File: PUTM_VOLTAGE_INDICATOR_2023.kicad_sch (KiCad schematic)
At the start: 29 parts

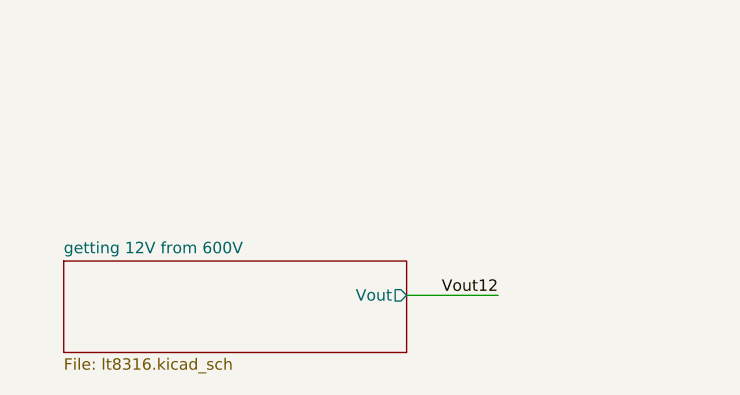
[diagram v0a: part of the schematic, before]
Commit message: change scheme of LT8316EFE and change mosfet symbol
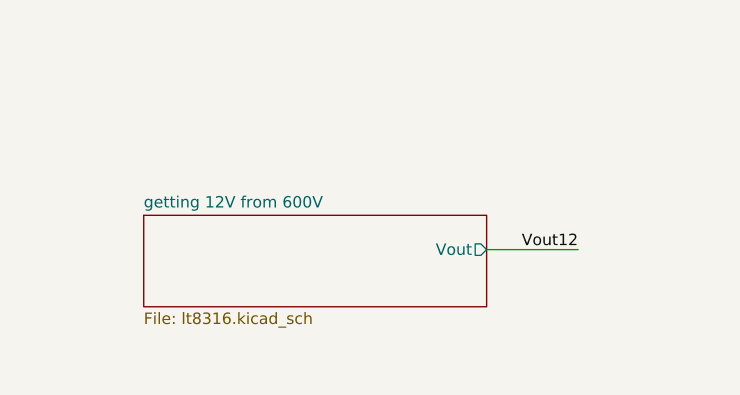
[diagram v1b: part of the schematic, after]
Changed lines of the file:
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@@
     (stroke (width 0) (type default) (color 0 0 0 0))
   )
-  (wire (pts (xy 57.15 175.26) (xy 67.31 175.26))
+  (wire (pts (xy 66.04 170.18) (xy 76.2 170.18))
     (stroke (width 0) (type default) (color 0 0 0 0))
   )
@@
     (effects (font (size 1.27 1.27)) (justify left bottom))
   )
-  (label "Vout12" (at 67.31 175.26 180)
+  (label "Vout12" (at 76.2 170.18 180)
     (effects (font (size 1.27 1.27)) (justify right bottom))
   )
@@
     (pin "1")
   )
-  (sheet (at 19.05 171.45) (size 38.1 10.16) (fields_autoplaced)
+  (sheet (at 27.94 166.37) (size 38.1 10.16) (fields_autoplaced)
     (stroke (width 0.1524) (type solid) (color 0 0 0 0))
     (fill (color 0 0 0 0.0000))
-    (property "Sheet name" "getting 12V from 600V" (id 0) (at 19.05 170.7384 0)
+    (property "Sheet name" "getting 12V from 600V" (id 0) (at 27.94 165.6584 0)
       (effects (font (size 1.27 1.27)) (justify left bottom))
     )
-    (property "Sheet file" "lt8316.kicad_sch" (id 1) (at 19.05 182.1946 0)
+    (property "Sheet file" "lt8316.kicad_sch" (id 1) (at 27.94 177.1146 0)
       (effects (font (size 1.27 1.27)) (justify left top))
     )
-    (pin "Vout" output (at 57.15 175.26 0)
+    (pin "Vout" output (at 66.04 170.18 0)
       (effects (font (size 1.27 1.27)) (justify right))
     )
@@
       (reference "#PWR?") (unit 1) (value "GND") (footprint "")
     )
+    (path "/cf374e18-b903-43ca-958b-fca5770ec61b/32e7c143-cc70-4ac4-97f7-77453f5f7f07"
+      (reference "#PWR?") (unit 1) (value "+VDC") (footprint "")
+    )
     (path "/4223f3f4-088d-4b9a-b16e-54b98ff9a1d3"
       (reference "#PWR?") (unit 1) (value "GND") (footprint "")
@@
       (reference "#PWR?") (unit 1) (value "+VDC") (footprint "")
     )
+    (path "/cf374e18-b903-43ca-958b-fca5770ec61b/558f1925-db51-40a5-9371-69be9ca78e10"
+      (reference "#PWR?") (unit 1) (value "GND") (footprint "")
+    )
     (path "/5b7feee9-3e0b-4567-88f5-c7d252aaf5c0"
       (reference "#PWR?") (unit 1) (value "+12V") (footprint "")
@@
       (reference "#PWR?") (unit 1) (value "+VDC") (footprint "")
     )
+    (path "/cf374e18-b903-43ca-958b-fca5770ec61b/c72ad2c8-75bd-4a1b-9496-8153431a76dd"
+      (reference "#PWR?") (unit 1) (value "GND") (footprint "")
+    )
     (path "/c838fd6c-06c5-492d-89ac-1fd1fa3897d4"
       (reference "#PWR?") (unit 1) (value "VCC") (footprint "")
@@
       (reference "#PWR?") (unit 1) (value "+12V") (footprint "")
     )
+    (path "/cf374e18-b903-43ca-958b-fca5770ec61b/e4996a15-9c7b-44e3-b2f2-01f8284846b2"
+      (reference "#PWR?") (unit 1) (value "GND") (footprint "")
+    )
     (path "/ec6155d8-6db3-4a50-a687-efa4cf3fb9c6"
       (reference "#PWR?") (unit 1) (value "GND") (footprint "")
@@
       (reference "0.1uF") (unit 1) (value "C") (footprint "")
     )
+    (path "/cf374e18-b903-43ca-958b-fca5770ec61b/6512fcfd-0e88-4a57-9170-2b4d1e9e185a"
+      (reference "0.1uF?") (unit 1) (value "C") (footprint "")
+    )
     (path "/2274b550-aef8-4476-a118-58107d10741d"
       (reference "C?") (unit 1) (value "2.2uF") (footprint "")
@@
       (reference "C?") (unit 1) (value "47uF") (footprint "")
     )
+    (path "/cf374e18-b903-43ca-958b-fca5770ec61b/3f6bfd71-6bce-4c99-bd68-922bfb83a1da"
+      (reference "C?") (unit 1) (value "10pF") (footprint "")
+    )
     (path "/cf374e18-b903-43ca-958b-fca5770ec61b/5056d3f2-c6d3-443f-aecd-c9ebfef5539c"
       (reference "C?") (unit 1) (value "100nF") (footprint "")
     )
+    (path "/cf374e18-b903-43ca-958b-fca5770ec61b/5b976bcd-7fe6-40cf-8a91-d330470a592a"
+      (reference "C?") (unit 1) (value "10uF") (footprint "")
+    )
     (path "/cf374e18-b903-43ca-958b-fca5770ec61b/5efacf5a-b103-469c-a71d-d6ed6b95c45d"
       (reference "C?") (unit 1) (value "100nF") (footprint "")
     )
+    (path "/cf374e18-b903-43ca-958b-fca5770ec61b/684025e0-d0bc-41d1-a713-7deaab9e1633"
+      (reference "C?") (unit 1) (value "47uF") (footprint "")
+    )
+    (path "/cf374e18-b903-43ca-958b-fca5770ec61b/cf62173b-3dc5-412e-a328-851c9eba7807"
+      (reference "C?") (unit 1) (value "100nF") (footprint "")
+    )
     (path "/cf374e18-b903-43ca-958b-fca5770ec61b/e533f7c5-34c4-4513-9f24-ddd1ccb1d81b"
       (reference "C?") (unit 1) (value "10pF") (footprint "")
@@
       (reference "C?") (unit 1) (value "2.2uF") (footprint "")
     )
+    (path "/cf374e18-b903-43ca-958b-fca5770ec61b/f3af4538-1c61-4dec-818c-ecf361cf4188"
+      (reference "C?") (unit 1) (value "100nF") (footprint "")
+    )
     (path "/cf374e18-b903-43ca-958b-fca5770ec61b/fd856d70-a228-45b6-bafe-4244511b43da"
       (reference "C?") (unit 1) (value "10uF") (footprint "")
@@
       (reference "D?") (unit 1) (value "DIODE") (footprint "")
     )
+    (path "/cf374e18-b903-43ca-958b-fca5770ec61b/8e24397d-5de2-4ffb-a482-80bf7b206b39"
+      (reference "D?") (unit 1) (value "US1K") (footprint "Diode_SMD:D_SMA")
+    )
     (path "/91897ede-6f44-4f3e-aa25-9e44a9bcbc0d"
       (reference "D?") (unit 1) (value "LED") (footprint "")
     )
+    (path "/cf374e18-b903-43ca-958b-fca5770ec61b/92a4bb15-3c41-4d86-8b01-0ce002af70c1"
+      (reference "D?") (unit 1) (value "US1K") (footprint "Diode_SMD:D_SMA")
+    )
     (path "/ad476781-3f83-4b0d-82bb-63d05393dcea"
       (reference "D?") (unit 1) (value "D_Zener") (footprint "")
@@
       (reference "D?") (unit 1) (value "LED") (footprint "")
     )
+    (path "/cf374e18-b903-43ca-958b-fca5770ec61b/e2426266-66c6-45c2-82b1-8cb37a277731"
+      (reference "D?") (unit 1) (value "DIODE") (footprint "")
+    )
     (path "/efffbf78-2a23-4c71-89c2-7b09495fb248"
       (reference "D?") (unit 1) (value "D_Zener") (footprint "")
@@
       (reference "D?") (unit 1) (value "US1K") (footprint "Diode_SMD:D_SMA")
     )
+    (path "/cf374e18-b903-43ca-958b-fca5770ec61b/dad6d136-bd1e-4494-a1d6-f69b7f63bdfa"
+      (reference "L?") (unit 1) (value "1mH") (footprint "")
+    )
     (path "/cf374e18-b903-43ca-958b-fca5770ec61b/facf2856-bf45-43c5-94eb-6ba4df7ce070"
       (reference "L?") (unit 1) (value "1mH") (footprint "")
@@
       (reference "M?") (unit 1) (value "MNMOS") (footprint "")
     )
+    (path "/cf374e18-b903-43ca-958b-fca5770ec61b/b886016f-513c-4ed6-805b-d3c85529adcb"
+      (reference "Q?") (unit 1) (value "Q_NMOS_GDS") (footprint "")
+    )
+    (path "/cf374e18-b903-43ca-958b-fca5770ec61b/0bf5e8c6-420a-4108-b6af-a1516a599ae1"
+      (reference "R?") (unit 1) (value "21.5k") (footprint "")
+    )
     (path "/0d6327f9-c706-469d-93b9-6ed83cf7370d"
       (reference "R?") (unit 1) (value "R4=300k") (footprint "")
@@
       (reference "R?") (unit 1) (value "22.1k") (footprint "")
     )
+    (path "/cf374e18-b903-43ca-958b-fca5770ec61b/3998addc-a70c-46f9-a60b-b4a696d22e54"
+      (reference "R?") (unit 1) (value "220mR") (footprint "")
+    )
+    (path "/cf374e18-b903-43ca-958b-fca5770ec61b/4cd7afc4-aeab-4fee-84c8-105654ee0db5"
+      (reference "R?") (unit 1) (value "2.49kR") (footprint "")
+    )
     (path "/cf374e18-b903-43ca-958b-fca5770ec61b/6215538f-5043-4302-9cc2-a18e15893de7"
       (reference "R?") (unit 1) (value "10kR") (footprint "")
@@
       (reference "R?") (unit 1) (value "R2=300k") (footprint "")
     )
+    (path "/cf374e18-b903-43ca-958b-fca5770ec61b/9e265a50-cd33-44ce-b896-405684d13d0c"
+      (reference "R?") (unit 1) (value "10kR") (footprint "")
+    )
     (path "/cf374e18-b903-43ca-958b-fca5770ec61b/9f4fddab-3d79-4c7c-97ad-d1227094eaff"
       (reference "R?") (unit 1) (value "220mR") (footprint "")
@@
       (reference "R?") (unit 1) (value "R3=100k") (footprint "")
     )
+    (path "/cf374e18-b903-43ca-958b-fca5770ec61b/a7accbdf-0597-40b2-9a61-7b33f248f0ff"
+      (reference "R?") (unit 1) (value "22.1k") (footprint "")
+    )
     (path "/ade8ddfd-444b-447a-8c15-b4c75b49afa4"
       (reference "R?") (unit 1) (value "10kR") (footprint "")
@@
       (reference "U?") (unit 1) (value "OPAMP") (footprint "")
     )
+    (path "/cf374e18-b903-43ca-958b-fca5770ec61b/5a37aa80-6a33-41f2-8f70-b377198a3006"
+      (reference "U?") (unit 1) (value "LT8316EFE") (footprint "TSSOP20_FE_BB_16_")
+    )
     (path "/6f6314b0-2ff3-49a8-aa6a-e4a7bd5d24fe"

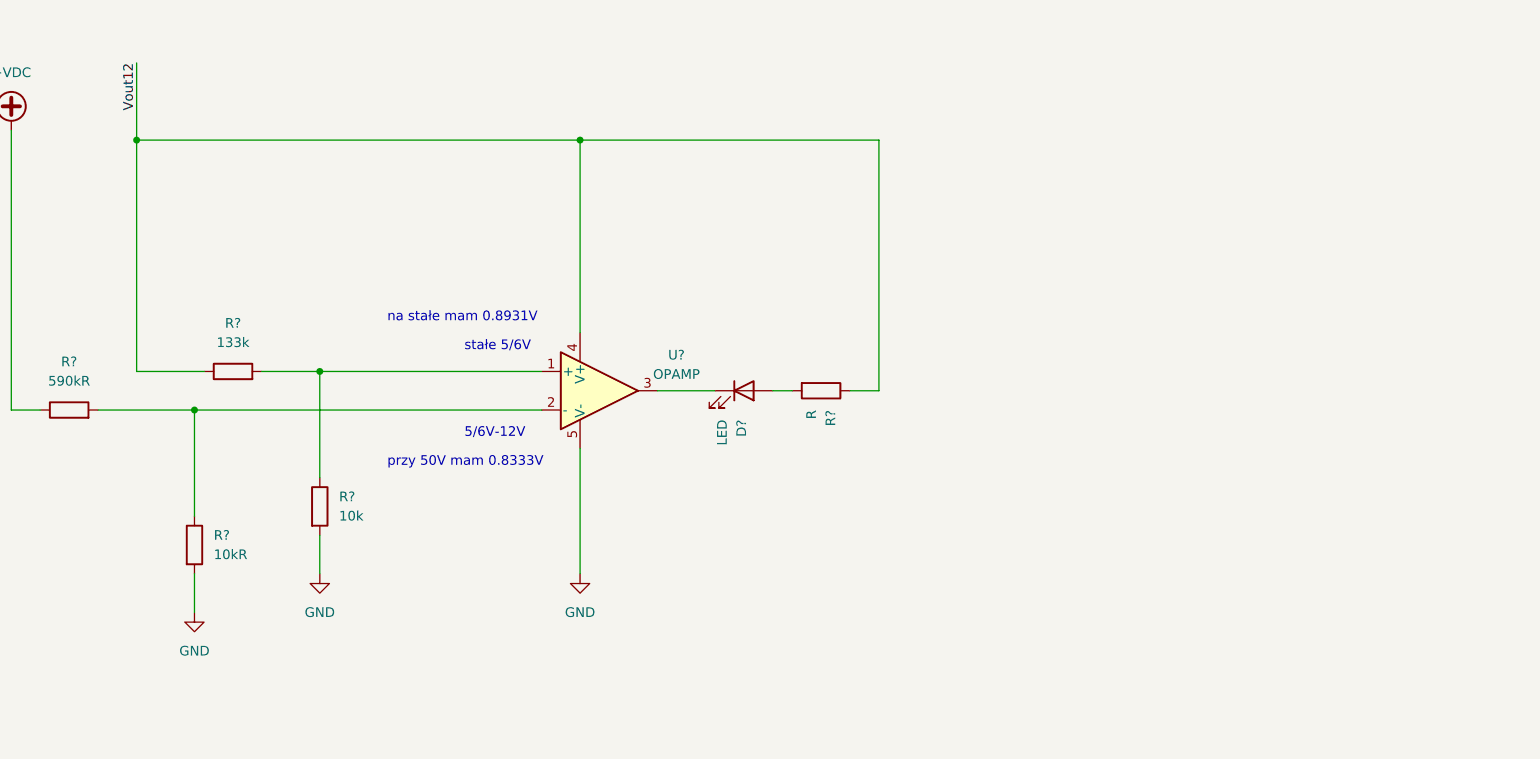
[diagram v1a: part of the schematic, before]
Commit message: add all the needed components
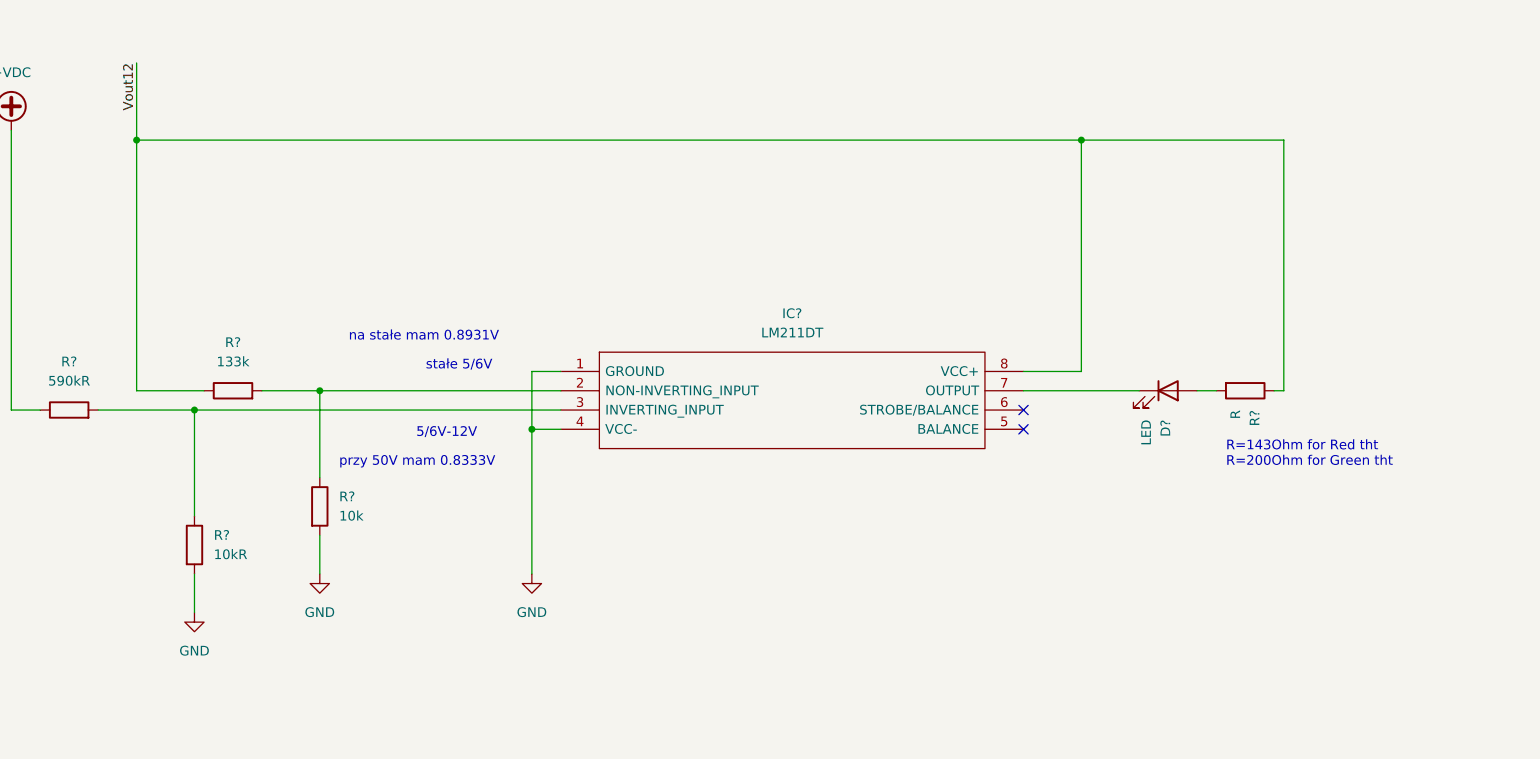
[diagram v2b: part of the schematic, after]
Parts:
- removed U?: OPAMP, symbol pspice:OPAMP
- added IC?: LM211DT, SOIC127P600X175-8N, symbol Voltage_indicator:LM211DT
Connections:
- net GND: now also IC?.1 (GROUND), IC?.4 (VCC-)
- net Vout12: now also IC?.8 (VCC+)
- net at R?.1, R?.2: now also IC?.3 (INVERTING_INPUT)
- net at R?.1, R?.2: now also IC?.2 (NON-INVERTING_INPUT)
- net at D?.1 (K): now also IC?.7 (OUTPUT)
- no-connect marks 0 -> 2
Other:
- note added: "R=143Ohm for Red tht R=200Ohm for Green tht"
- moved on the sheet: D?, R?

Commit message: gitignore change + capacitors improve
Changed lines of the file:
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@@
   (junction (at 119.38 96.52) (diameter 0) (color 0 0 0 0)
   )
-  (junction (at 95.25 63.5) (diameter 0) (color 0 0 0 0)
-  )
   (junction (at 144.78 -52.07) (diameter 0) (color 0 0 0 0)
   )
@@
   (junction (at 27.94 -92.71) (diameter 0) (color 0 0 0 0)
   )
+  (junction (at 219.71 76.2) (diameter 0) (color 0 0 0 0)
+  )
   (junction (at 41.91 -92.71) (diameter 0) (color 0 0 0 0)
   )
   (junction (at 193.04 -82.55) (diameter 0) (color 0 0 0 0)
   )
-  (junction (at 219.71 63.5) (diameter 0) (color 0 0 0 0)
+  (junction (at 95.25 76.2) (diameter 0) (color 0 0 0 0)
   )
   (junction (at 144.78 -82.55) (diameter 0) (color 0 0 0 0)
@@
     (stroke (width 0) (type default) (color 0 0 0 0))
   )
-  (wire (pts (xy 95.25 63.5) (xy 219.71 63.5))
+  (wire (pts (xy 95.25 76.2) (xy 219.71 76.2))
     (stroke (width 0) (type default) (color 0 0 0 0))
   )
@@
     (stroke (width 0) (type default) (color 0 0 0 0))
   )
-  (wire (pts (xy 219.71 93.98) (xy 219.71 63.5))
+  (wire (pts (xy 95.25 76.2) (xy 95.25 96.52))
+    (stroke (width 0) (type default) (color 0 0 0 0))
+  )
+  (wire (pts (xy 219.71 93.98) (xy 219.71 76.2))
     (stroke (width 0) (type default) (color 0 0 0 0))
   )
@@
     (stroke (width 0) (type default) (color 0 0 0 0))
   )
-  (wire (pts (xy 95.25 63.5) (xy 95.25 53.34))
+  (wire (pts (xy 95.25 53.34) (xy 95.25 76.2))
     (stroke (width 0) (type default) (color 0 0 0 0))
   )
@@
     (stroke (width 0) (type default) (color 0 0 0 0))
   )
-  (wire (pts (xy 95.25 63.5) (xy 95.25 96.52))
-    (stroke (width 0) (type default) (color 0 0 0 0))
-  )
   (wire (pts (xy 257.81 -69.85) (xy 255.27 -69.85))
     (stroke (width 0) (type default) (color 0 0 0 0))
@@
     (stroke (width 0) (type default) (color 0 0 0 0))
   )
-  (wire (pts (xy 219.71 63.5) (xy 246.38 63.5))
+  (wire (pts (xy 219.71 76.2) (xy 246.38 76.2))
     (stroke (width 0) (type default) (color 0 0 0 0))
   )
@@
     (stroke (width 0) (type default) (color 0 0 0 0))
   )
-  (wire (pts (xy 246.38 63.5) (xy 246.38 96.52))
+  (wire (pts (xy 246.38 76.2) (xy 246.38 96.52))
     (stroke (width 0) (type default) (color 0 0 0 0))
   )
@@
       (reference "C?") (unit 1) (value "100nF") (footprint "")
     )
-    (path "/cf374e18-b903-43ca-958b-fca5770ec61b/dce9d68b-1d1e-45fe-87bf-7022f3a10da4"
-      (reference "C?") (unit 1) (value "47uF") (footprint "")
-    )
     (path "/cf374e18-b903-43ca-958b-fca5770ec61b/e533f7c5-34c4-4513-9f24-ddd1ccb1d81b"
       (reference "C?") (unit 1) (value "10pF") (footprint "")
@@
       (reference "C?") (unit 1) (value "100nF") (footprint "")
     )
+    (path "/cf374e18-b903-43ca-958b-fca5770ec61b/f42b809d-9243-41cb-9698-6d3e40ec152e"
+      (reference "C?") (unit 1) (value "47uF") (footprint "")
+    )
     (path "/cf374e18-b903-43ca-958b-fca5770ec61b/fd856d70-a228-45b6-bafe-4244511b43da"
